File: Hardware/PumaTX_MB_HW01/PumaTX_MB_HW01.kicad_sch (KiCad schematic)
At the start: 87 parts, among them J1 PSoM_ESP32S2_Carrier_Board, J100 FH12A-26S-0.5SH_55_, J102 500334-0160, J103 500334-0160, J104 692122030100, J105 53398-0667, J2 FFC2B28-12-G, J3 U.FL-R-SMT-1_40_, J400 U.FL-R-SMT-1_40_, M130 Motor_DC, M140 Fan, Q130 ZXMN3B01F, Q140 ZXMN3B01F, U1 74HC165BQ,115, U2 74HC165BQ,115, U3 SX1280, U400 ESP32-PICO-D4, U402 E28-2G4M27S, U520 MIC5528-3.3YMT-T5, U530 MIC5528-3.3YMT-T5, Y1 NX2016SA-52MHZ-EXS00A-CS06016

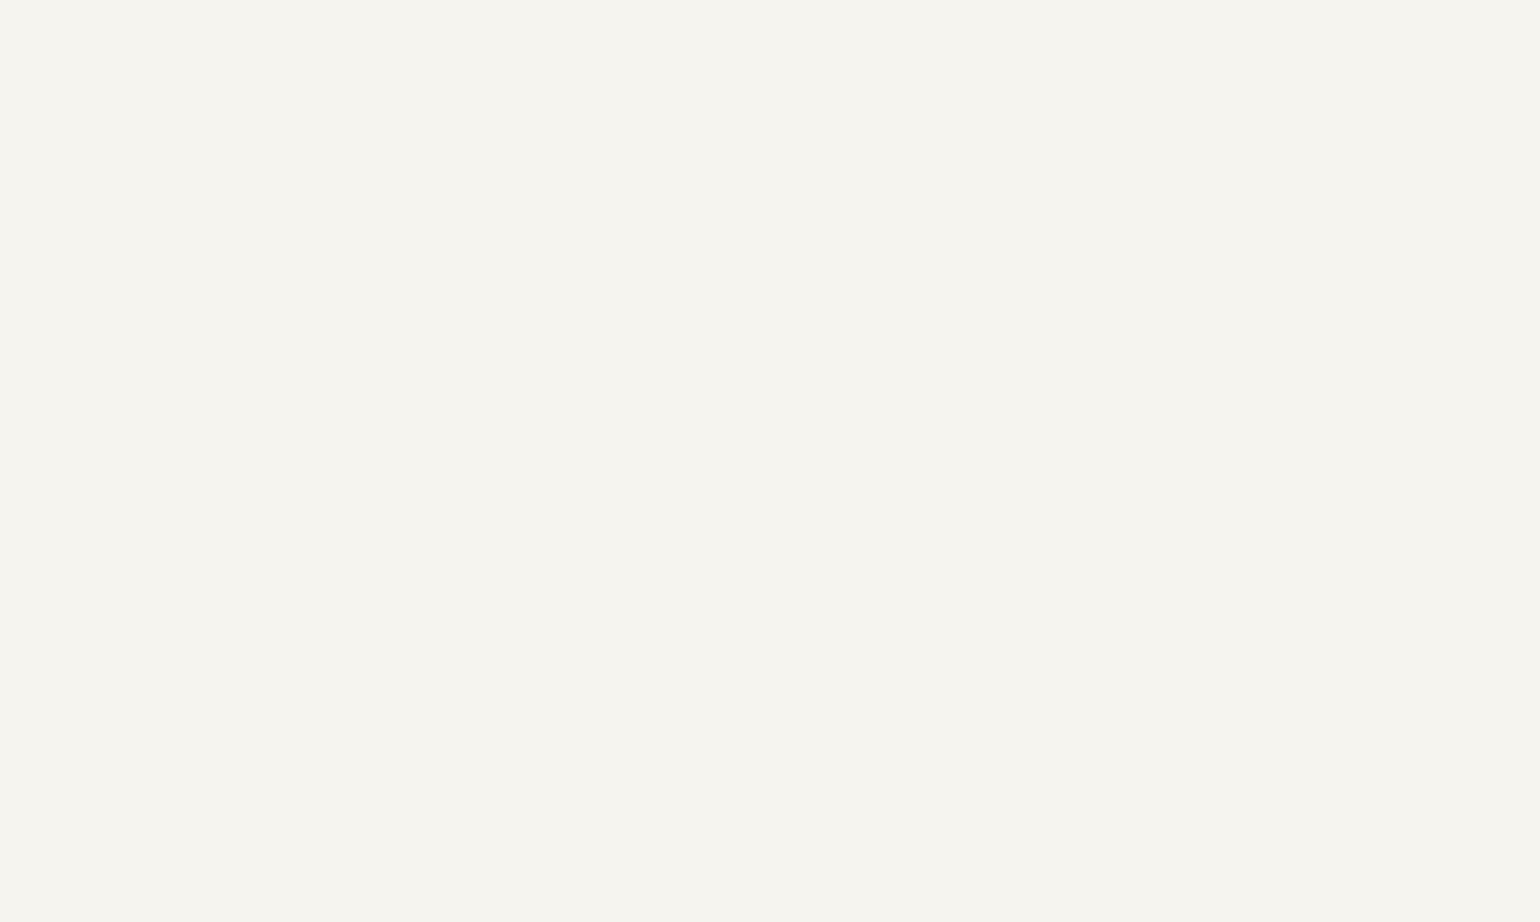
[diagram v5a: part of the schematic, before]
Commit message: started schematics of LR1121
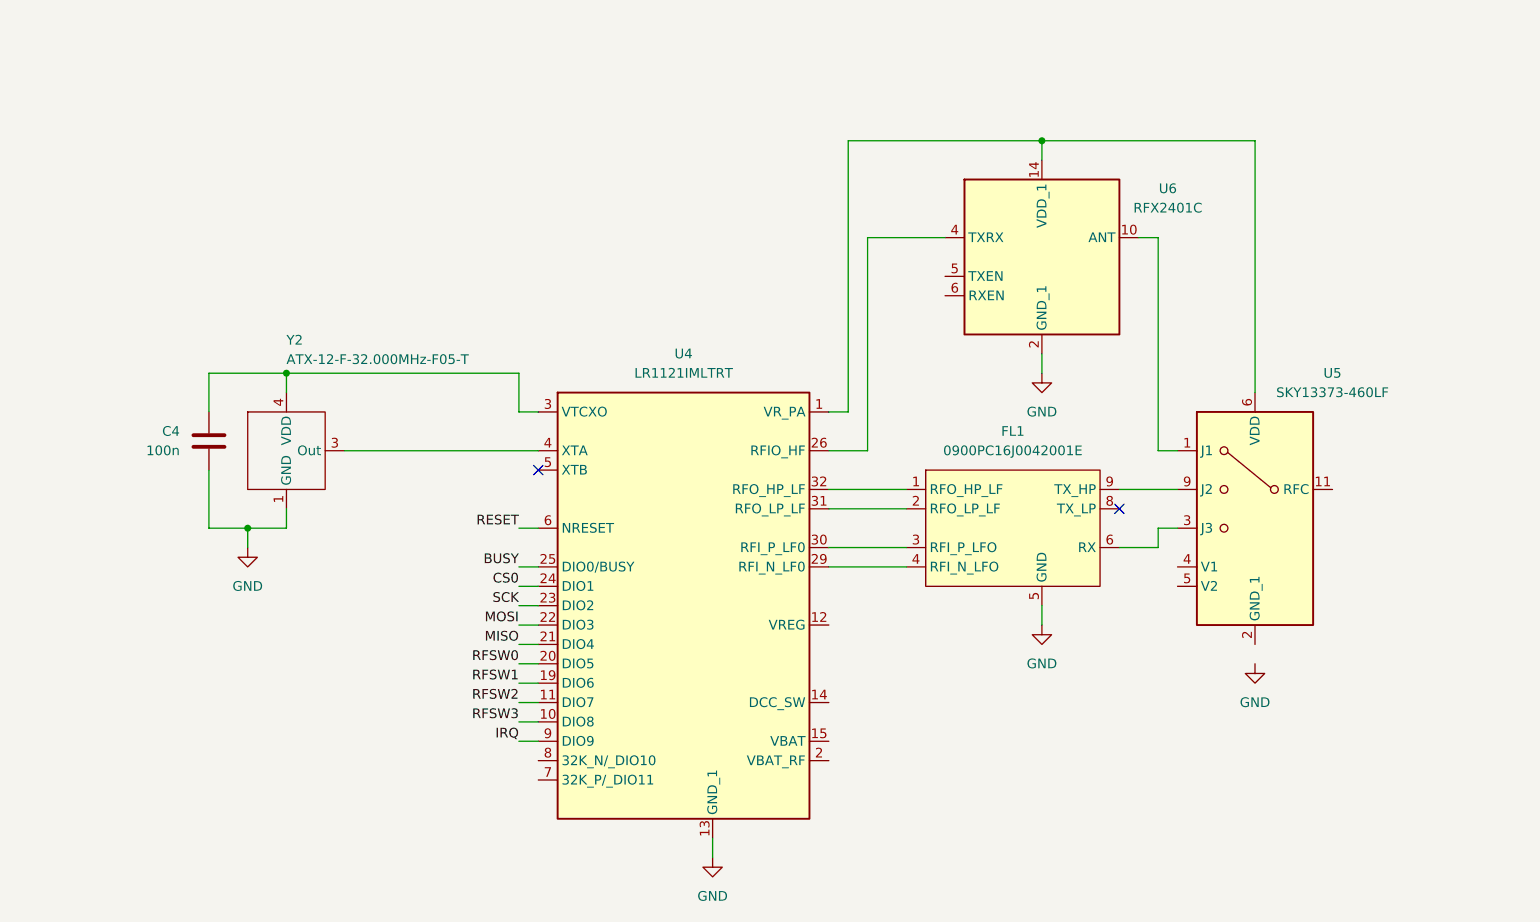
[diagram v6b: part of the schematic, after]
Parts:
- added C4: 100n, symbol Component_lib:C
- added FL1: 0900PC16J0042001E, symbol Component_lib:0900PC16J0042001E
- added U4: LR1121IMLTRT, Component_lib:QFN50P500X500X100-33N-D, symbol Component_lib:LR1121IMLTRT
- added U5: SKY13373-460LF, QFN50P200X200X60-13N-D, symbol Component_lib:SKY13373-460LF
- added U6: RFX2401C, Component_lib:QFN50P300X300X60-17N-D, symbol Component_lib:RFX2401C
- added Y2: ATX-12-F-32.000MHz-F05-T, Component_lib:ATX12F32000MHZF05T, symbol Component_lib:ATX-12-F-32.000MHz-F05-T
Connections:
- net BUSY: now also U4.25 (DIO0/BUSY)
- net GND: now also C4.1, FL1.10 (GND), FL1.5 (GND), FL1.7 (GND), U4.13 (GND_1), U4.33 (GND_2), U6.11 (GND_5), U6.17 (GND_6), U6.2 (GND_1), U6.3 (GND_2), U6.8 (GND_3), U6.9 (GND_4), Y2.1 (GND), Y2.2 (GND)
- net MISO: now also U4.21 (DIO4)
- net MOSI: now also U4.22 (DIO3)
- net SCK: now also U4.23 (DIO2)
- new net: C4.2, U4.3 (VTCXO), Y2.4 (VDD)
- new net: FL1.1 (RFO_HP_LF), U4.32 (RFO_HP_LF)
- new net: FL1.2 (RFO_LP_LF), U4.31 (RFO_LP_LF)
- new net: FL1.3 (RFI_P_LFO), U4.30 (RFI_P_LF0)
- new net: FL1.4 (RFI_N_LFO), U4.29 (RFI_N_LF0)
- new net: FL1.6 (RX), U5.3 (J3)
- new net: FL1.9 (TX_HP), U5.9 (J2)
- new net: U5.1 (J1), U6.10 (ANT)
- new net: U4.1 (VR_PA), U5.6 (VDD), U6.14 (VDD_1), U6.16 (VDD_2)
- new net: U4.26 (RFIO_HF), U6.4 (TXRX)
- new net: U4.16 (DNC_1), U4.17 (DNC_2), U4.18 (DNC_3), U4.27 (DNC_4), U4.28 (DNC_5)
- new net: U4.4 (XTA), Y2.3 (Out)
- new net: U5.10 (GND_4), U5.12 (GND_5), U5.13 (EPAD), U5.2 (GND_1), U5.7 (GND_2), U5.8 (GND_3)
- new net CS0: U4.24 (DIO1)
- new net IRQ: U4.9 (DIO9)
- new net RESET: U4.6 (NRESET)
- new net RFSW0: U4.20 (DIO5)
- new net RFSW1: U4.19 (DIO6)
- new net RFSW2: U4.11 (DIO7)
- new net RFSW3: U4.10 (DIO8)
- no-connect marks 50 -> 52

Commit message: Update PumaTX_MB_HW01.kicad_sch
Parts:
- added J4: U.FL-R-SMT-1_40_, Component_lib:u.fl, symbol Component_lib:U.FL-R-SMT-1_40_
- added U7: BGSA14GN10E6327XTSA1, Component_lib:BGSA14GN10E6327XTSA1, symbol Component_lib:BGSA14GN10E6327XTSA1
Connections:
- net BUSY: no longer U4.25 (DIO0/BUSY)
- net GND: now also U5.10 (GND_4), U5.12 (GND_5), U5.13 (EPAD), U5.2 (GND), U5.7 (GND_2), U5.8 (GND_3), J4.2 (gnd)
- net MISO: no longer U4.21 (DIO4)
- net MOSI: no longer U4.22 (DIO3)
- net SCK: no longer U4.23 (DIO2)
- net RADIO_VTCXO_1: now reaches C4.2, U4.3 (VTCXO), Y2.4 (VDD)
- net RFO_HP_LF_1: now reaches FL1.1 (RFO_HP_LF), U4.32 (RFO_HP_LF)
- net RFO_LP_LF_1: now reaches FL1.2 (RFO_LP_LF), U4.31 (RFO_LP_LF)
- net RFI_P_LF_1: now reaches FL1.3 (RFI_P_LFO), U4.30 (RFI_P_LF0)
- net RFI_N_LF_1: now reaches FL1.4 (RFI_N_LFO), U4.29 (RFI_N_LF0)
- net RX_LF_1: now reaches FL1.6 (RX), U5.3 (J3)
- net TX_HP_LF_1: now reaches FL1.9 (TX_HP), U5.9 (J2)
- net at U6.1 (N/C_1): now also U6.12 (N/C_3), U6.13 (DNC), U6.15 (N/C_4), U6.7 (N/C_2)
- net HP_HF_1: now reaches U5.1 (J1), U6.10 (ANT)
- net RADIO_VR_PA_1: now reaches U4.1 (VR_PA), U5.6 (VDD), U6.14 (VDD), U6.16 (VDD_2)
- net LP_HF_1: now reaches U4.26 (RFIO_HF), U6.4 (TXRX)
- net RADIO_XTA_1: now reaches U4.4 (XTA), Y2.3 (Out)
- net RF_OUT_1: now reaches U5.11 (RFC)
- net RF_OUT_1: now also J4.1 (ant)
- net CS0 renamed RADIO_CS0_1
- net IRQ renamed RADIO_IRQ_1
- net RESET renamed RADIO_RESET_1
- net RFSW0 renamed RADIO_RFSW0_1
- net RFSW1 renamed RADIO_RFSW1_1
- net RFSW2 renamed RADIO_RFSW2_1
- net RFSW3 renamed RADIO_RFSW3_1
- new net: U7.3 (GND), U7.7 (GND_2)
- new net RADIO_BUSY_1: U4.25 (DIO0/BUSY)
- new net RADIO_MISO_1: U4.21 (DIO4)
- new net RADIO_MOSI_1: U4.22 (DIO3)
- new net RADIO_SCK_1: U4.23 (DIO2)
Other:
- moved on the sheet: FL1, U5, U6
